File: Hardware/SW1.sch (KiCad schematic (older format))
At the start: 6 parts, among them SW1 SW_Rotary2x4

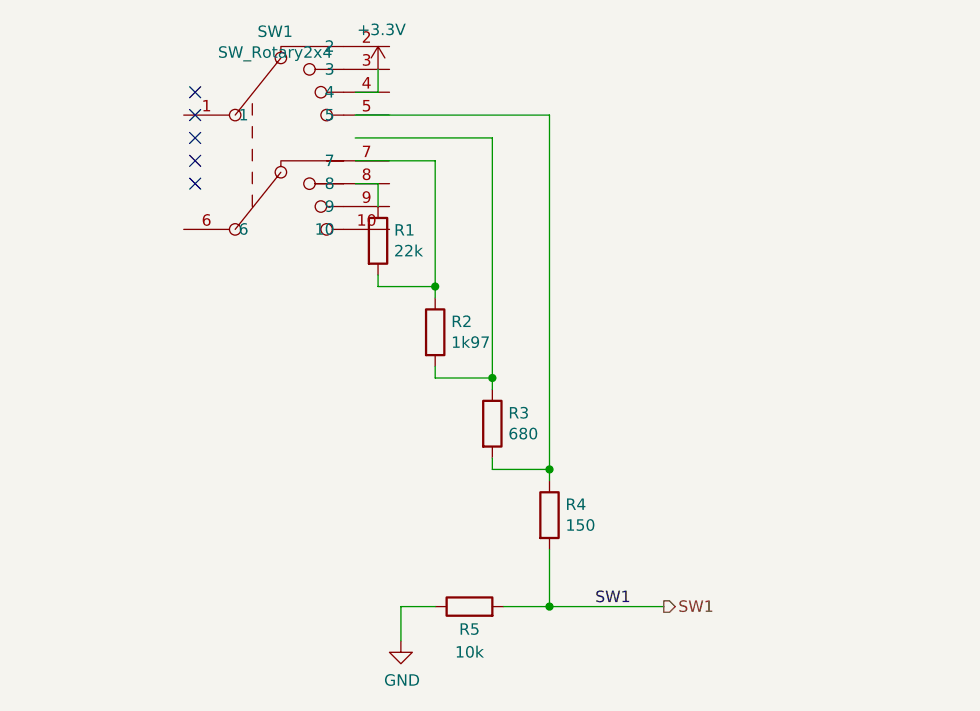
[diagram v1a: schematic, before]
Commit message: symbol changed, bigger cable hole in the middle
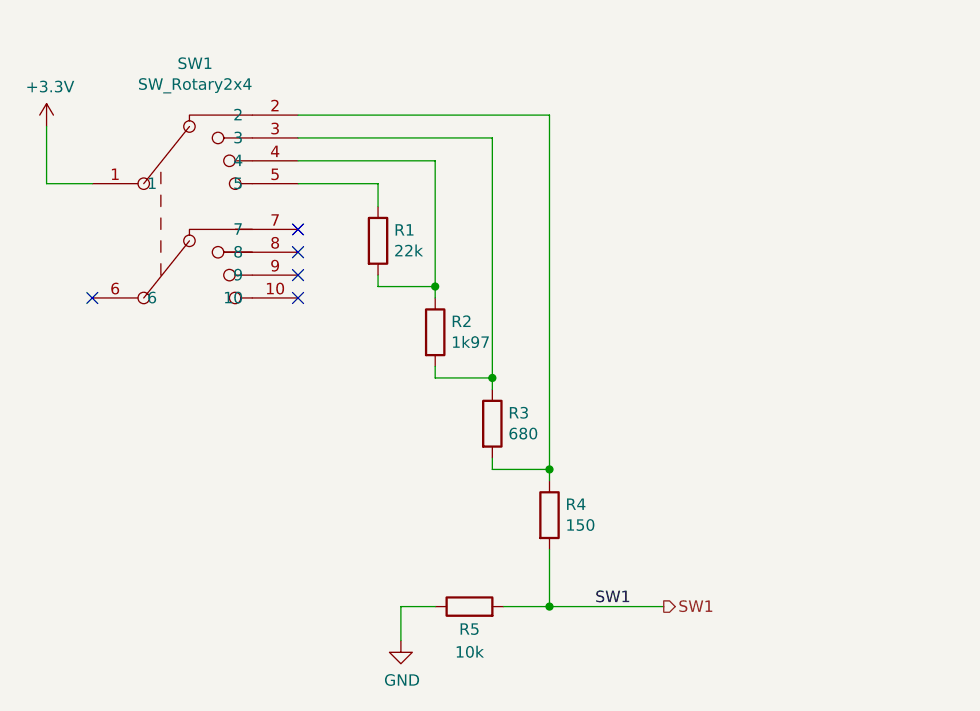
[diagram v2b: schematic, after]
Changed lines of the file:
@@
 $EndDescr
 $Comp
-L Switch:SW_Rotary2x4 SW1
-U 1 1 61B7ED93
-P 6900 3450
-F 0 "SW1" H 6900 3865 50  0000 C CNN
-F 1 "SW_Rotary2x4" H 6900 3774 50  0000 C CNN
-F 2 "Rotary_Encoder:SW_Rotary2x4" H 6950 3900 50  0001 C CNN
-F 3 "https://www.piekarz.pl/21583-przelacznik-kh10-obrotowy-bistabilny-4xon-4-pozycje/" H 6950 3900 50  0001 C CNN
-	1    6900 3450
-	1    0    0    -1
-$EndComp
-$Comp
 L Device:R R1
 U 1 1 61B7F45F
@@
 L power:+3.3V #PWR0102
 U 1 1 61B80122
-P 7350 3200
-F 0 "#PWR0102" H 7350 3050 50  0001 C CNN
-F 1 "+3.3V" H 7365 3373 50  0000 C CNN
-F 2 "" H 7350 3200 50  0001 C CNN
-F 3 "" H 7350 3200 50  0001 C CNN
-	1    7350 3200
+P 5900 3450
+F 0 "#PWR0102" H 5900 3300 50  0001 C CNN
+F 1 "+3.3V" H 5915 3623 50  0000 C CNN
+F 2 "" H 5900 3450 50  0001 C CNN
+F 3 "" H 5900 3450 50  0001 C CNN
+	1    5900 3450
 	1    0    0    -1
 $EndComp
-Wire Wire Line
-	7350 3200 7350 3300
-Wire Wire Line
-	7350 3300 7250 3300
 $Comp
 L Device:R R2
@@
 	7600 4200 7600 4150
 Wire Wire Line
-	7600 4150 7350 4150
-Wire Wire Line
 	7350 4150 7350 4100
 Wire Wire Line
 	7350 3800 7350 3700
 Wire Wire Line
-	7350 3700 7250 3700
-Wire Wire Line
 	7600 4150 7600 3600
-Wire Wire Line
-	7600 3600 7250 3600
 Connection ~ 7600 4150
 Wire Wire Line
-	7250 3500 7850 3500
-Wire Wire Line
 	7850 3500 7850 4550
 Connection ~ 7850 4550
 Wire Wire Line
 	8100 4950 8100 3400
-Wire Wire Line
-	8100 3400 7250 3400
 Connection ~ 8100 4950
 Connection ~ 8100 5550
@@
 Wire Wire Line
 	8100 5550 8600 5550
-NoConn ~ 6550 3300
-NoConn ~ 6550 3400
-NoConn ~ 6550 3500
-NoConn ~ 6550 3600
-NoConn ~ 6550 3700
 $Bitmap
-Pos 3950 3650
+Pos 3100 3950
 Scale 1.000000
 Data
@@
 EndData
 $EndBitmap
+$Comp
+L Switch:SW_Rotary2x4 SW1
+U 1 1 61CD50C9
+P 6500 3750
+F 0 "SW1" H 6550 4325 50  0000 C CNN
+F 1 "SW_Rotary2x4" H 6550 4234 50  0000 C CNN
+F 2 "Rotary_Encoder:SW_Rotary2x4" H 6550 4400 50  0001 C CNN
+F 3 "https://www.piekarz.pl/21583-przelacznik-kh10-obrotowy-bistabilny-4xon-4-pozycje/" H 6550 4400 50  0001 C CNN
+	1    6500 3750
+	1    0    0    -1
+$EndComp
+Wire Wire Line
+	7350 4150 7600 4150
+Wire Wire Line
+	7000 3400 8100 3400
+Wire Wire Line
+	7000 3500 7850 3500
+Wire Wire Line
+	7000 3600 7600 3600
+Wire Wire Line
+	7000 3700 7350 3700
+Wire Wire Line
+	5900 3450 5900 3700
+Wire Wire Line
+	5900 3700 6100 3700
+NoConn ~ 6100 4200
+NoConn ~ 7000 3900
+NoConn ~ 7000 4000
+NoConn ~ 7000 4100
+NoConn ~ 7000 4200
 $EndSCHEMATC

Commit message: redesigned PCB
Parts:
- SW1: symbol Switch:SW_Rotary2x4 -> KieraV2-rescue:SW_Rotary2x4-Switch
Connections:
- net +3V3: now also SW1.13; no longer SW1.1
- net at R1.1: now also SW1.4; no longer SW1.5
- net at R1.2, R2.1: now also SW1.3; no longer SW1.4
- net at R2.2, R3.1: now also SW1.2; no longer SW1.3
- net at R3.2, R4.1: now also SW1.1; no longer SW1.2
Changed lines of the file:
@@
 $EndBitmap
 $Comp
-L Switch:SW_Rotary2x4 SW1
+L KieraV2-rescue:SW_Rotary2x4-Switch SW1
 U 1 1 61CD50C9
 P 6500 3750
+AR Path="/61CD50C9" Ref="SW1"  Part="1"
+AR Path="/61B7E6EB/61CD50C9" Ref="SW1"  Part="1"
 F 0 "SW1" H 6550 4325 50  0000 C CNN
 F 1 "SW_Rotary2x4" H 6550 4234 50  0000 C CNN

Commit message: wip
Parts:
- SW1: symbol KieraV2-rescue:SW_Rotary2x4-Switch -> Switch:SW_Rotary2x4
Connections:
- net +3V3: now also SW1.1; no longer SW1.13
- net at R1.1: now also SW1.5; no longer SW1.4
- net at R1.2, R2.1: now also SW1.4; no longer SW1.3
- net at R2.2, R3.1: now also SW1.3; no longer SW1.2
- net at R3.2, R4.1: now also SW1.2; no longer SW1.1
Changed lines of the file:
@@
 $EndBitmap
 $Comp
-L KieraV2-rescue:SW_Rotary2x4-Switch SW1
+L Switch:SW_Rotary2x4 SW1
 U 1 1 61CD50C9
 P 6500 3750

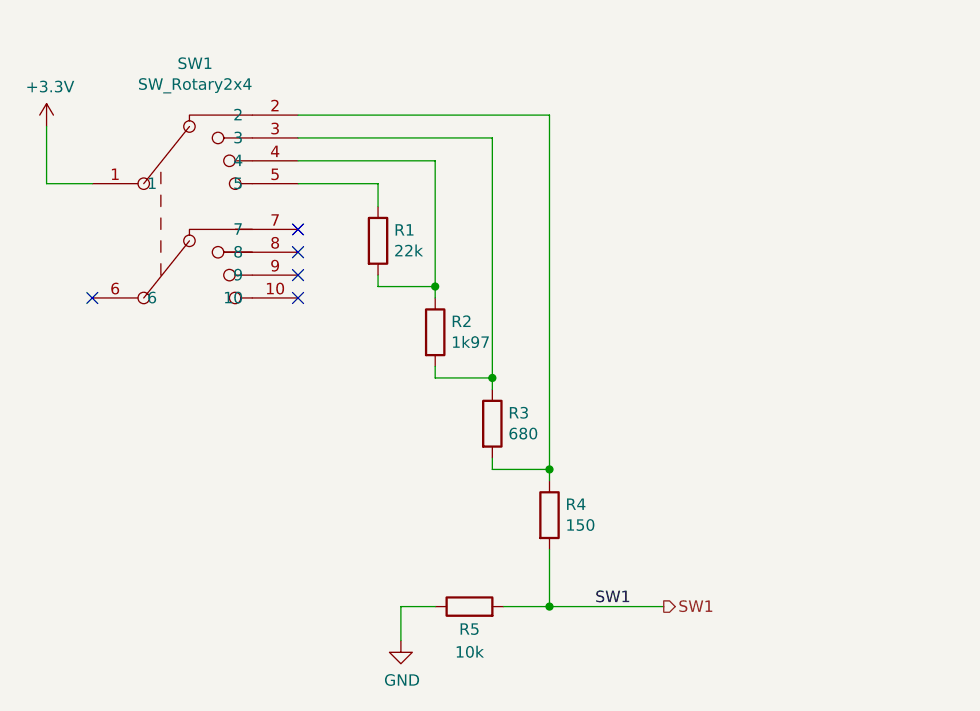
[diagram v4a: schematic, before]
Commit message: removed resistor ladder
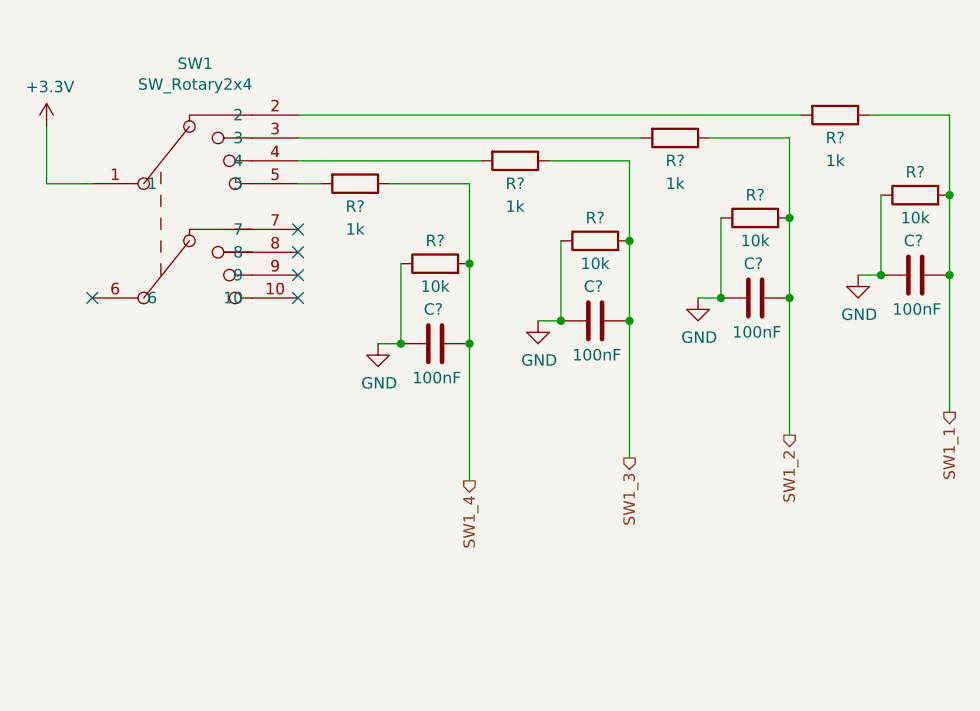
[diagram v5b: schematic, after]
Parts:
- removed R1: 22k, Resistor_SMD:R_0603_1608Metric, symbol Device:R
- removed R2: 1k97, Resistor_SMD:R_0603_1608Metric, symbol Device:R
- removed R3: 680, Resistor_SMD:R_0603_1608Metric, symbol Device:R
- removed R4: 150, Resistor_SMD:R_0603_1608Metric, symbol Device:R
- removed R5: 10k, Resistor_SMD:R_0603_1608Metric, symbol Device:R
- added C? (x4): 100nF, Capacitor_SMD:C_0603_1608Metric, symbol Device:C
- added R? (x4): 10k, Resistor_SMD:R_0603_1608Metric, symbol Device:R
- added R? (x4): 1k, Resistor_SMD:R_0603_1608Metric, symbol Device:R
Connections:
- net GND: now also C?.2, C?.2, C?.2, C?.2, R?.1, R?.1, R?.1, R?.1
- net at SW1.5: now also R?.2
- net at SW1.4: now also R?.2
- net at SW1.3: now also R?.2
- net at SW1.2: now also R?.2
- new net SW1_1: C?.1, R?.1, R?.2
- new net SW1_2: C?.1, R?.1, R?.2
- new net SW1_3: C?.1, R?.1, R?.2
- new net SW1_4: C?.1, R?.1, R?.2

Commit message: added more buttons
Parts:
- gave numbers to parts that had none: 12
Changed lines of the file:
@@
 U 1 1 6297EAAE
 P 7600 4050
-F 0 "R?" V 7700 4050 50  0000 C CNN
+AR Path="/61B9B4C0/6297EAAE" Ref="R?"  Part="1"
+AR Path="/61B7E6EB/6297EAAE" Ref="R2"  Part="1"
+F 0 "R2" V 7700 4050 50  0000 C CNN
 F 1 "10k" V 7500 4050 50  0000 C CNN
 F 2 "Resistor_SMD:R_0603_1608Metric" V 7530 4050 50  0001 C CNN
@@
 P 7350 4400
 AR Path="/61B9B4C0/6297EAB4" Ref="#PWR?"  Part="1"
-AR Path="/61B7E6EB/6297EAB4" Ref="#PWR?"  Part="1"
-F 0 "#PWR?" H 7350 4150 50  0001 C CNN
+AR Path="/61B7E6EB/6297EAB4" Ref="#PWR015"  Part="1"
+F 0 "#PWR015" H 7350 4150 50  0001 C CNN
 F 1 "GND" H 7355 4227 50  0000 C CNN
 F 2 "" H 7350 4400 50  0001 C CNN
@@
 U 1 1 6297EABD
 P 7250 3700
-F 0 "R?" V 7350 3700 50  0000 C CNN
+AR Path="/61B9B4C0/6297EABD" Ref="R?"  Part="1"
+AR Path="/61B7E6EB/6297EABD" Ref="R1"  Part="1"
+F 0 "R1" V 7350 3700 50  0000 C CNN
 F 1 "1k" V 7450 3700 50  0000 C CNN
 F 2 "Resistor_SMD:R_0603_1608Metric" V 7180 3700 50  0001 C CNN
@@
 U 1 1 6297EAC3
 P 7600 4400
-F 0 "C?" V 7450 4350 50  0000 L CNN
+AR Path="/61B9B4C0/6297EAC3" Ref="C?"  Part="1"
+AR Path="/61B7E6EB/6297EAC3" Ref="C23"  Part="1"
+F 0 "C23" V 7450 4350 50  0000 L CNN
 F 1 "100nF" V 7750 4300 50  0000 L CNN
 F 2 "Capacitor_SMD:C_0603_1608Metric" H 7638 4250 50  0001 C CNN
@@
 U 1 1 62992590
 P 8300 3950
-F 0 "R?" V 8400 3950 50  0000 C CNN
+AR Path="/61B9B4C0/62992590" Ref="R?"  Part="1"
+AR Path="/61B7E6EB/62992590" Ref="R4"  Part="1"
+F 0 "R4" V 8400 3950 50  0000 C CNN
 F 1 "10k" V 8200 3950 50  0000 C CNN
 F 2 "Resistor_SMD:R_0603_1608Metric" V 8230 3950 50  0001 C CNN
@@
 P 8050 4300
 AR Path="/61B9B4C0/62992596" Ref="#PWR?"  Part="1"
-AR Path="/61B7E6EB/62992596" Ref="#PWR?"  Part="1"
-F 0 "#PWR?" H 8050 4050 50  0001 C CNN
+AR Path="/61B7E6EB/62992596" Ref="#PWR016"  Part="1"
+F 0 "#PWR016" H 8050 4050 50  0001 C CNN
 F 1 "GND" H 8055 4127 50  0000 C CNN
 F 2 "" H 8050 4300 50  0001 C CNN
@@
 U 1 1 6299259F
 P 7950 3600
-F 0 "R?" V 8050 3600 50  0000 C CNN
+AR Path="/61B9B4C0/6299259F" Ref="R?"  Part="1"
+AR Path="/61B7E6EB/6299259F" Ref="R3"  Part="1"
+F 0 "R3" V 8050 3600 50  0000 C CNN
 F 1 "1k" V 8150 3600 50  0000 C CNN
 F 2 "Resistor_SMD:R_0603_1608Metric" V 7880 3600 50  0001 C CNN
@@
 U 1 1 629925A5
 P 8300 4300
-F 0 "C?" V 8150 4250 50  0000 L CNN
+AR Path="/61B9B4C0/629925A5" Ref="C?"  Part="1"
+AR Path="/61B7E6EB/629925A5" Ref="C24"  Part="1"
+F 0 "C24" V 8150 4250 50  0000 L CNN
 F 1 "100nF" V 8450 4200 50  0000 L CNN
 F 2 "Capacitor_SMD:C_0603_1608Metric" H 8338 4150 50  0001 C CNN
@@
 U 1 1 62993CC6
 P 9000 3850
-F 0 "R?" V 9100 3850 50  0000 C CNN
+AR Path="/61B9B4C0/62993CC6" Ref="R?"  Part="1"
+AR Path="/61B7E6EB/62993CC6" Ref="R6"  Part="1"
+F 0 "R6" V 9100 3850 50  0000 C CNN
 F 1 "10k" V 8900 3850 50  0000 C CNN
 F 2 "Resistor_SMD:R_0603_1608Metric" V 8930 3850 50  0001 C CNN
@@
 P 8750 4200
 AR Path="/61B9B4C0/62993CCC" Ref="#PWR?"  Part="1"
-AR Path="/61B7E6EB/62993CCC" Ref="#PWR?"  Part="1"
-F 0 "#PWR?" H 8750 3950 50  0001 C CNN
+AR Path="/61B7E6EB/62993CCC" Ref="#PWR020"  Part="1"
+F 0 "#PWR020" H 8750 3950 50  0001 C CNN
 F 1 "GND" H 8755 4027 50  0000 C CNN
 F 2 "" H 8750 4200 50  0001 C CNN
@@
 U 1 1 62993CD5
 P 8650 3500
-F 0 "R?" V 8750 3500 50  0000 C CNN
+AR Path="/61B9B4C0/62993CD5" Ref="R?"  Part="1"
+AR Path="/61B7E6EB/62993CD5" Ref="R5"  Part="1"
+F 0 "R5" V 8750 3500 50  0000 C CNN
 F 1 "1k" V 8850 3500 50  0000 C CNN
 F 2 "Resistor_SMD:R_0603_1608Metric" V 8580 3500 50  0001 C CNN
@@
 U 1 1 62993CDB
 P 9000 4200
-F 0 "C?" V 8850 4150 50  0000 L CNN
+AR Path="/61B9B4C0/62993CDB" Ref="C?"  Part="1"
+AR Path="/61B7E6EB/62993CDB" Ref="C25"  Part="1"
+F 0 "C25" V 8850 4150 50  0000 L CNN
 F 1 "100nF" V 9150 4100 50  0000 L CNN
 F 2 "Capacitor_SMD:C_0603_1608Metric" H 9038 4050 50  0001 C CNN
@@
 U 1 1 62994DF1
 P 9700 3750
-F 0 "R?" V 9800 3750 50  0000 C CNN
+AR Path="/61B9B4C0/62994DF1" Ref="R?"  Part="1"
+AR Path="/61B7E6EB/62994DF1" Ref="R8"  Part="1"
+F 0 "R8" V 9800 3750 50  0000 C CNN
 F 1 "10k" V 9600 3750 50  0000 C CNN
 F 2 "Resistor_SMD:R_0603_1608Metric" V 9630 3750 50  0001 C CNN
@@
 P 9450 4100
 AR Path="/61B9B4C0/62994DF7" Ref="#PWR?"  Part="1"
-AR Path="/61B7E6EB/62994DF7" Ref="#PWR?"  Part="1"
-F 0 "#PWR?" H 9450 3850 50  0001 C CNN
+AR Path="/61B7E6EB/62994DF7" Ref="#PWR021"  Part="1"
+F 0 "#PWR021" H 9450 3850 50  0001 C CNN
 F 1 "GND" H 9455 3927 50  0000 C CNN
 F 2 "" H 9450 4100 50  0001 C CNN
@@
 U 1 1 62994E00
 P 9350 3400
-F 0 "R?" V 9450 3400 50  0000 C CNN
+AR Path="/61B9B4C0/62994E00" Ref="R?"  Part="1"
+AR Path="/61B7E6EB/62994E00" Ref="R7"  Part="1"
+F 0 "R7" V 9450 3400 50  0000 C CNN
 F 1 "1k" V 9550 3400 50  0000 C CNN
 F 2 "Resistor_SMD:R_0603_1608Metric" V 9280 3400 50  0001 C CNN
@@
 U 1 1 62994E06
 P 9700 4100
-F 0 "C?" V 9550 4050 50  0000 L CNN
+AR Path="/61B9B4C0/62994E06" Ref="C?"  Part="1"
+AR Path="/61B7E6EB/62994E06" Ref="C26"  Part="1"
+F 0 "C26" V 9550 4050 50  0000 L CNN
 F 1 "100nF" V 9850 4000 50  0000 L CNN
 F 2 "Capacitor_SMD:C_0603_1608Metric" H 9738 3950 50  0001 C CNN
